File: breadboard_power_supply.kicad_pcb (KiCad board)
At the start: 2 copper layers, 75.2 x 54.4 mm, 27 parts, among them J1 PJ-059AH, J10 Conn_01x04, J11 Conn_01x12_Male, J12 Conn_01x04, J13 Conn_01x04_Male, J14 Conn_01x04, J2 Conn_01x07, J3 Conn_01x08, J4 Screw_Terminal_01x06, J5 Conn_01x04_Male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

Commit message: Redesign of the PCB
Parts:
- C1, C2, C3: footprint Capacitor_SMD:C_0805_2012Metric -> Capacitor_THT:C_Disc_D3.0mm_W2.0mm_P2.50mm
- D1: footprint LED_SMD:LED_0805_2012Metric -> LED_THT:LED_D5.0mm
- R1, R2, R3, R4, R5: footprint Resistor_SMD:R_0805_2012Metric -> Resistor_THT:R_Axial_DIN0204_L3.6mm_D1.6mm_P7.62mm_Horizontal
- moved C2 29.1 mm to (55.2, 131.4)
- moved D1 23.9 mm to (55.0, 124.9)
- moved C3 20.2 mm to (47.0, 147.1)
- moved C1 19.8 mm to (51.4, 131.4), turned to 180 degrees
- moved R2 16.9 mm to (70.7, 156.7), turned to 180 degrees
- moved R1 5.85 mm to (52.4, 150.4)
- moved R3 1.58 mm to (59.8, 156.6)
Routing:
- net /VCCB: track 201.0 -> 161.8 mm
- net /12V: track 60.4 -> 27.2 mm
- net Net-(R1-Pad1): track 16.2 -> 0.00 mm, vias 2 -> 0
- net Net-(D1-Pad2): track 11.7 -> 0.00 mm
- net /Connectors/Rx: track 9.88 -> 0.00 mm
- net /A0_MQ131: track 74.5 -> 78.7 mm
- net /VCCA: track 183.2 -> 185.4 mm
- net GND: track 83.3 -> 85.4 mm, vias 7 -> 2

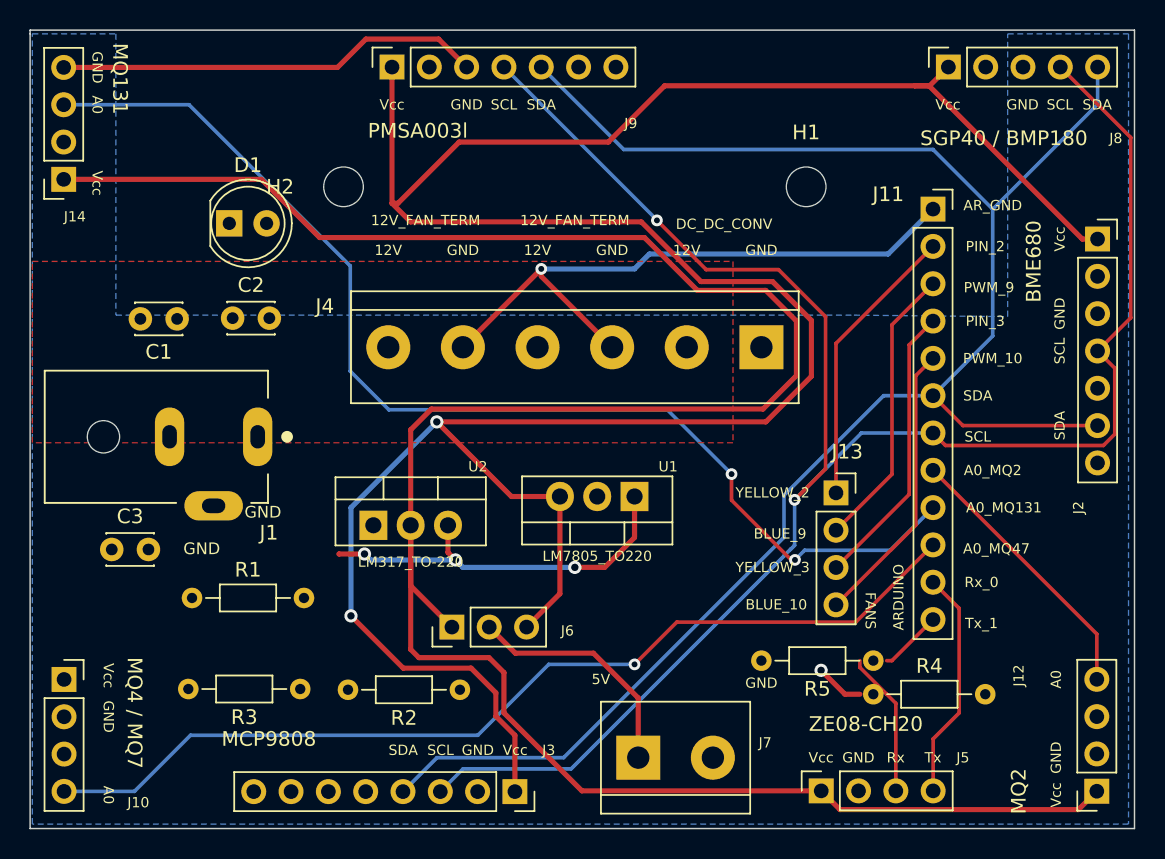
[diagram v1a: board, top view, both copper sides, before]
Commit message: Everything THT before deleting the space marking lines
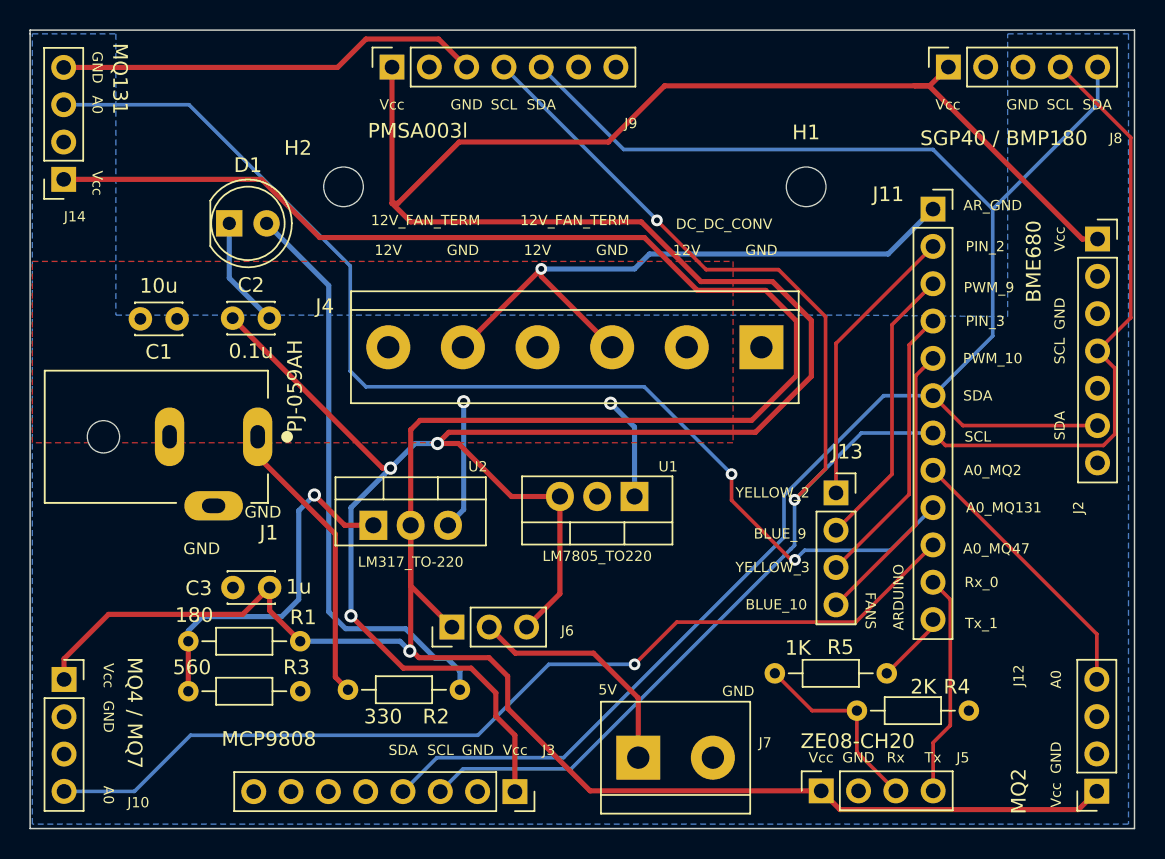
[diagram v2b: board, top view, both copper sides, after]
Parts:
- moved C3 11.1 mm to (57.7, 149.7), turned to 180 degrees
- moved R4 6.60 mm to (105.3, 158.1), turned to 180 degrees
- moved R1 2.96 mm to (52.2, 153.4)
- moved R5 1.26 mm to (99.7, 155.5)
- moved R3 0.15 mm to (59.8, 156.8)
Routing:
- net Net-(D1-Pad2): track 0.00 -> 40.1 mm
- net /VCCB: track 161.8 -> 191.3 mm, vias 0 -> 1
- net Net-(R1-Pad1): track 0.00 -> 24.9 mm, vias 0 -> 1
- net /VCCA: track 185.4 -> 199.8 mm, vias 2 -> 3
- net /Connectors/Rx: track 0.00 -> 13.2 mm
- net /12V: track 27.2 -> 35.6 mm, vias 3 -> 2
- net GND: track 85.4 -> 79.8 mm, vias 2 -> 1
- net /Rx: track 4.31 -> 4.97 mm
